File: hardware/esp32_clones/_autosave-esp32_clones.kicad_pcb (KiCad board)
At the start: 2 copper layers, 110 x 60 mm, 27 parts, among them J2 USB_A, J3 USB_A, J4 USB_A, J5 Micro_SD_Card, J6 Barrel_Jack, J7 DA15_Pins, J9 AudioJack2_Ground

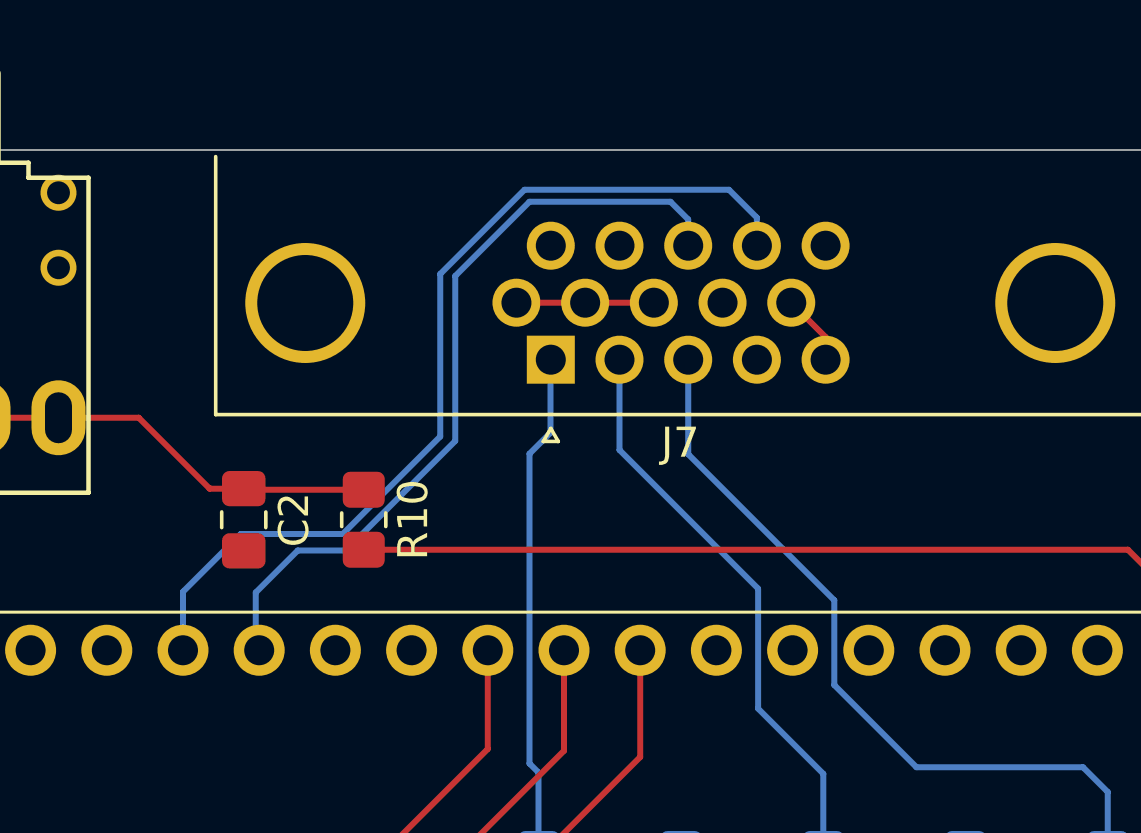
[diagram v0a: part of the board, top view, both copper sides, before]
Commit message: refactor: rebrand emulator modules for CP400
- rename emulator source files, headers, symbols, and menu text for CP400
- move project headers into the src directory
- standardize file banners and update copyright attribution
- correct VGA content centering using the active framebuffer dimensions
- reposition the F12 main menu within the visible VGA area
- update the VGA sync pin configuration for the ESP32-S3 board
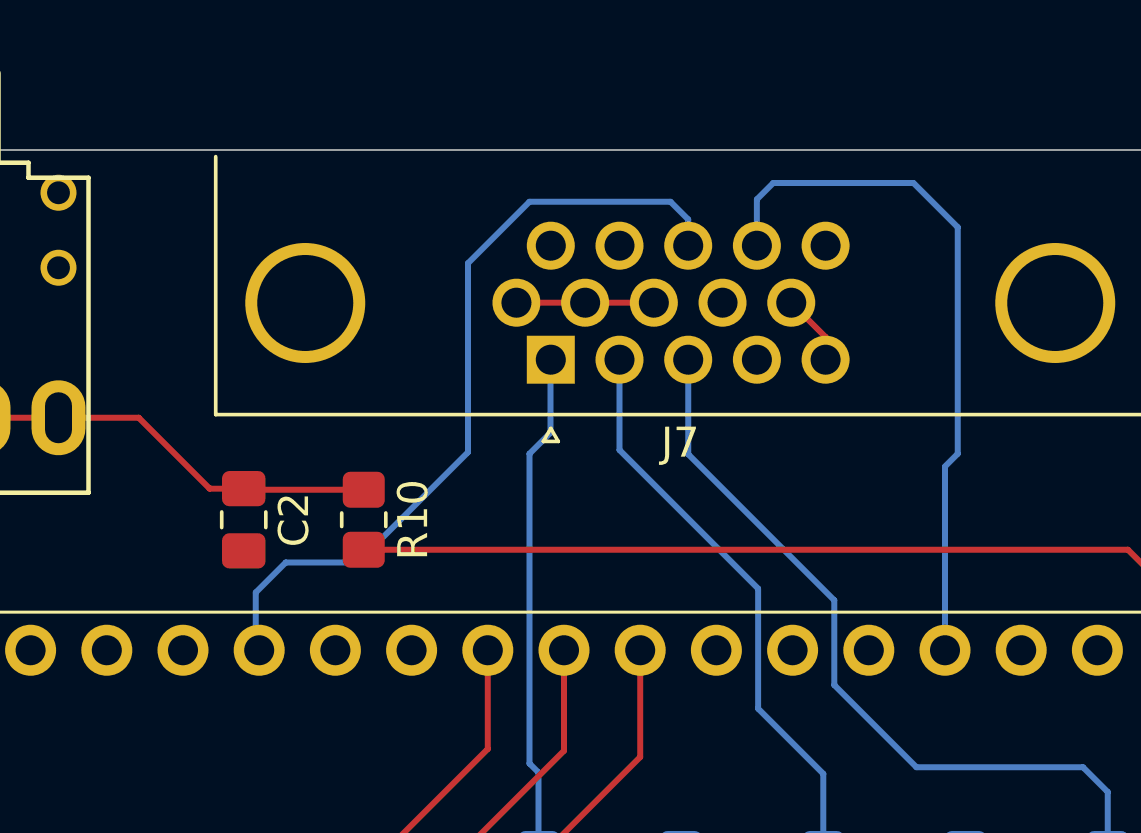
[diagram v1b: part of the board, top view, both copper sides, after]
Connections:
- U1 pad 19: Net-(J7-P14) -> unconnected-(U1-IO01-Pad19)
- U1 pad 9: unconnected-(U1-IO00-Pad9) -> Net-(J7-P14)
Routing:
- net Net-(J7-P14): track 31.1 -> 23.4 mm
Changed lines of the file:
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@@
 		(title "ESP32 Clones")
 		(date "2026-08-02")
-		(rev "1.1")
+		(rev "1.0")
 		(company "The Retro Hacker")
 		(comment 2 "Commercial-ShareAlike 4.0 Internacional License")
@@
 			(layers "*.Cu" "*.Mask")
 			(remove_unused_layers no)
-			(net "unconnected-(U1-IO00-Pad9)")
+			(net "Net-(J7-P14)")
 			(pinfunction "IO00_9")
-			(pintype "bidirectional+no_connect")
+			(pintype "bidirectional")
 		)
 		(pad "10" thru_hole circle
@@
 			(layers "*.Cu" "*.Mask")
 			(remove_unused_layers no)
-			(net "Net-(J7-P14)")
+			(net "unconnected-(U1-IO01-Pad19)")
 			(pinfunction "IO01_19")
-			(pintype "bidirectional")
+			(pintype "bidirectional+no_connect")
 		)
 		(pad "20" thru_hole circle
@@
 	)
 	(segment
-		(start 169.425 61.325)
-		(end 170.355 62.255)
+		(start 177.05 70.125)
+		(end 176.625 70.55)
 		(width 0.2)
 		(layer "B.Cu")
@@
 	)
 	(segment
-		(start 151.225 76.675)
-		(end 151.225 74.725)
+		(start 170.355 61.645)
+		(end 170.9 61.1)
 		(width 0.2)
 		(layer "B.Cu")
@@
 	)
 	(segment
-		(start 151.225 74.725)
-		(end 153.15 72.8)
+		(start 176.625 70.55)
+		(end 176.625 76.675)
 		(width 0.2)
 		(layer "B.Cu")
@@
 	)
 	(segment
-		(start 162.609315 61.325)
-		(end 169.425 61.325)
+		(start 170.355 63.19)
+		(end 170.355 61.645)
 		(width 0.2)
 		(layer "B.Cu")
@@
 	)
 	(segment
-		(start 153.15 72.8)
-		(end 156.55 72.8)
+		(start 170.9 61.1)
+		(end 175.575 61.1)
 		(width 0.2)
 		(layer "B.Cu")
@@
 	)
 	(segment
-		(start 156.55 72.8)
-		(end 159.8 69.55)
+		(start 177.05 62.575)
+		(end 177.05 70.125)
 		(width 0.2)
 		(layer "B.Cu")
@@
 	)
 	(segment
-		(start 170.355 62.255)
-		(end 170.355 63.19)
+		(start 175.575 61.1)
+		(end 177.05 62.575)
 		(width 0.2)
 		(layer "B.Cu")
@@
 	)
 	(segment
-		(start 159.8 69.55)
-		(end 159.8 64.134315)
-		(width 0.2)
-		(layer "B.Cu")
-		(net "Net-(J7-P14)")
-	)
-	(segment
-		(start 159.8 64.134315)
-		(end 162.609315 61.325)
-		(width 0.2)
-		(layer "B.Cu")
-		(net "Net-(J7-P14)")
-	)
-	(segment
-		(start 153.65 74.75)
-		(end 153.65 76.56)
+		(start 157.05 73.75)
+		(end 154.65 73.75)
 		(width 0.2)
 		(layer "B.Cu")
@@
 	)
 	(segment
-		(start 162.775 61.725)
-		(end 160.3 64.2)
+		(start 153.65 76.56)
+		(end 153.765 76.675)
 		(width 0.2)
 		(layer "B.Cu")
@@
 	)
 	(segment
-		(start 153.65 76.56)
-		(end 153.765 76.675)
+		(start 160.725 70.075)
+		(end 157.05 73.75)
 		(width 0.2)
 		(layer "B.Cu")
@@
 	)
 	(segment
-		(start 155.05 73.35)
+		(start 154.65 73.75)
 		(end 153.65 74.75)
 		(width 0.2)
@@
 	)
 	(segment
-		(start 160.3 64.2)
-		(end 160.3 69.7)
+		(start 162.775 61.725)
+		(end 160.725 63.775)
 		(width 0.2)
 		(layer "B.Cu")
@@
 	)
 	(segment
-		(start 168.065 63.19)
-		(end 168.065 62.315)
+		(start 160.725 63.775)
+		(end 160.725 70.075)
 		(width 0.2)
 		(layer "B.Cu")
@@
 	)
 	(segment
-		(start 156.65 73.35)
-		(end 155.05 73.35)
+		(start 168.065 62.315)
+		(end 167.475 61.725)
 		(width 0.2)
 		(layer "B.Cu")
@@
 	)
 	(segment
-		(start 167.475 61.725)
-		(end 162.775 61.725)
+		(start 153.65 74.75)
+		(end 153.65 76.56)
 		(width 0.2)
 		(layer "B.Cu")
@@
 	)
 	(segment
-		(start 160.3 69.7)
-		(end 156.65 73.35)
+		(start 167.475 61.725)
+		(end 162.775 61.725)
 		(width 0.2)
 		(layer "B.Cu")
@@
 	)
 	(segment
-		(start 168.065 62.315)
-		(end 167.475 61.725)
+		(start 168.065 63.19)
+		(end 168.065 62.315)
 		(width 0.2)
 		(layer "B.Cu")
